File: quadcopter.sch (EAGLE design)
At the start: 58 parts, among them J1 AVR_SPI_PRG_6NS, U1 ATMEGA128RFA1

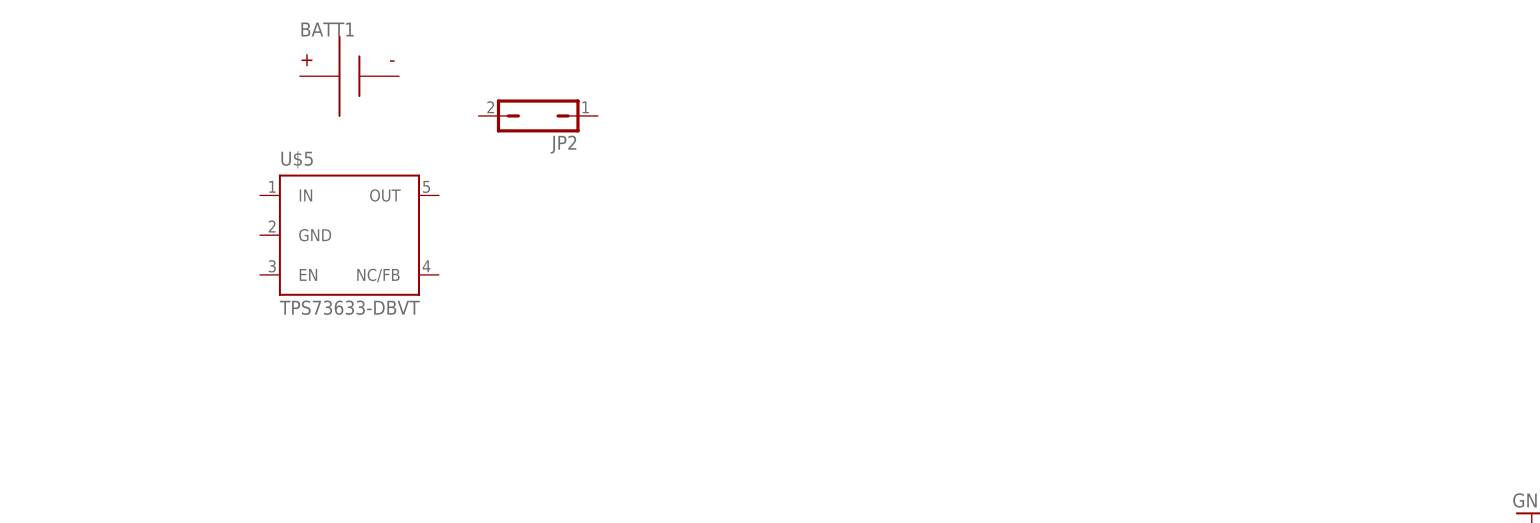
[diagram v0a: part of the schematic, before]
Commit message: Added breakout header and power-supply parts
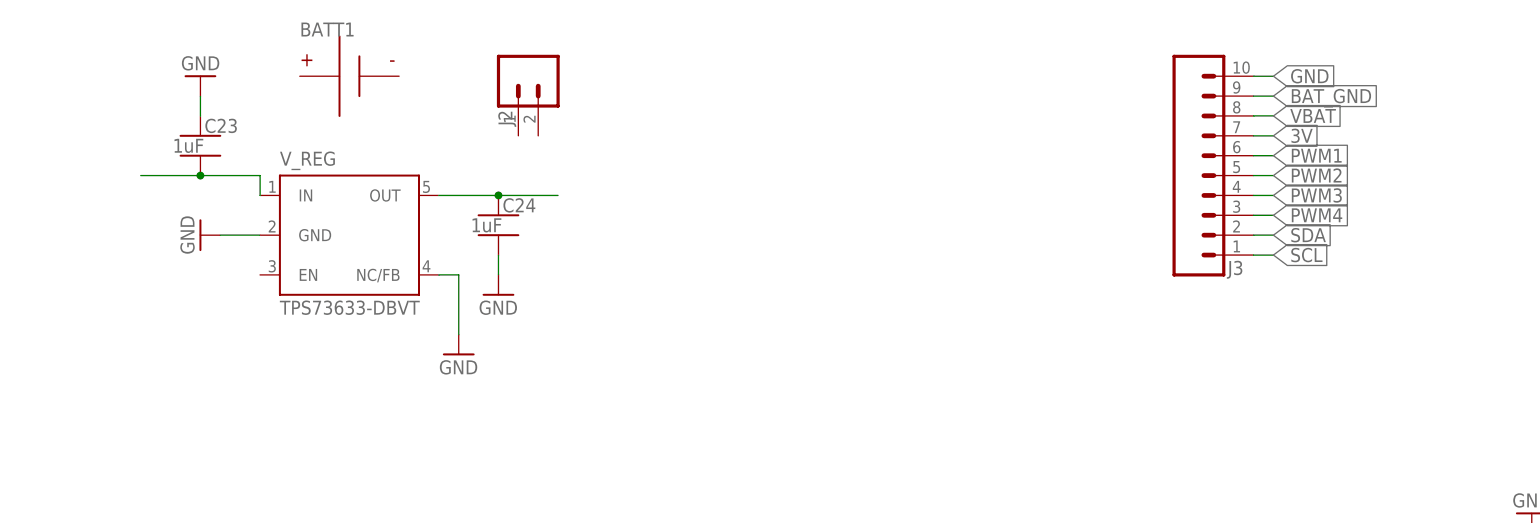
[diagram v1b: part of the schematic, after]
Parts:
- removed JP2: (no value), jumper:JP1Q
- added C23, C24: 1uF, quadparts_prebuilt:CAPACITOR-NP_SMD-2012-0805_CERAMIC-1UF
- added J2: (no value), quadparts-nick:MALE_HEADER_2POS-2X1-0.1IN
- added J3: (no value), quadparts_prebuilt:SIP-10_TH-254X10
- renumbered U$5 to V_REG
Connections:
- new net 3V: J3.7
- new net BAT_GND: J3.9
- new net N$16: C24.1, V_REG.OUT
- new net N$17: C23.2, V_REG.IN
- new net SCL: J3.1
- new net SDA: J3.2
- new net VBAT: J3.8
- net GND: now also C23.1, C24.2, J3.10, V_REG.GND, V_REG.NC/FB
- net PWM1: now also J3.6
- net PWM2: now also J3.5
- net PWM3: now also J3.4
- net PWM4: now also J3.3
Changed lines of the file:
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@@
 <part name="C20" library="quadparts_prebuilt" deviceset="CAPACITOR-NP_" device="SMD-2012-0805_CERAMIC-0.1UF" value="0.1uF"/>
 <part name="BATT1" library="quadparts_prebuilt" deviceset="BATTERY" device="-HUBSAN-W/HOLDER"/>
-<part name="U$5" library="quadparts_prebuilt" deviceset="TPS73633-DBVT" device=""/>
-<part name="JP2" library="jumper" deviceset="JP1Q" device=""/>
+<part name="V_REG" library="quadparts_prebuilt" deviceset="TPS73633-DBVT" device=""/>
+<part name="GND33" library="quadparts_prebuilt" deviceset="GND" device=""/>
+<part name="GND34" library="quadparts_prebuilt" deviceset="GND" device=""/>
+<part name="C23" library="quadparts_prebuilt" deviceset="CAPACITOR-NP_" device="SMD-2012-0805_CERAMIC-1UF" value="1uF"/>
+<part name="C24" library="quadparts_prebuilt" deviceset="CAPACITOR-NP_" device="SMD-2012-0805_CERAMIC-1UF" value="1uF"/>
+<part name="GND35" library="quadparts_prebuilt" deviceset="GND" device=""/>
+<part name="GND36" library="quadparts_prebuilt" deviceset="GND" device=""/>
+<part name="J2" library="quadparts-nick" deviceset="MALE_HEADER_2POS" device="-2X1-0.1IN"/>
+<part name="J3" library="quadparts_prebuilt" deviceset="SIP-10_" device="TH-254X10"/>
 </parts>
 <sheets>
@@
 <instance part="C20" gate="G$1" x="160.02" y="2.54"/>
 <instance part="BATT1" gate="G$1" x="-101.6" y="60.96"/>
-<instance part="U$5" gate="G$1" x="-111.76" y="33.02"/>
-<instance part="JP2" gate="A" x="-78.74" y="55.88" rot="R90"/>
+<instance part="V_REG" gate="G$1" x="-111.76" y="33.02"/>
+<instance part="GND33" gate="1" x="-121.92" y="40.64" rot="R270"/>
+<instance part="GND34" gate="1" x="-88.9" y="25.4"/>
+<instance part="C23" gate="G$1" x="-121.92" y="53.34"/>
+<instance part="C24" gate="G$1" x="-83.82" y="43.18"/>
+<instance part="GND35" gate="1" x="-121.92" y="60.96" rot="R180"/>
+<instance part="GND36" gate="1" x="-83.82" y="33.02"/>
+<instance part="J2" gate="G$1" x="-83.82" y="63.5" rot="R270"/>
+<instance part="J3" gate="G$1" x="2.54" y="35.56"/>
 </instances>
 <busses>
@@
 <wire x1="147.32" y1="-25.4" x2="147.32" y2="-27.94" width="0.1524" layer="91"/>
 </segment>
+<segment>
+<pinref part="GND33" gate="1" pin="GND"/>
+<pinref part="V_REG" gate="G$1" pin="GND"/>
+<wire x1="-119.38" y1="40.64" x2="-114.3" y2="40.64" width="0.1524" layer="91"/>
+</segment>
+<segment>
+<pinref part="V_REG" gate="G$1" pin="NC/FB"/>
+<pinref part="GND34" gate="1" pin="GND"/>
+<wire x1="-91.44" y1="35.56" x2="-88.9" y2="35.56" width="0.1524" layer="91"/>
+<wire x1="-88.9" y1="35.56" x2="-88.9" y2="27.94" width="0.1524" layer="91"/>
+</segment>
+<segment>
+<pinref part="C23" gate="G$1" pin="1"/>
+<pinref part="GND35" gate="1" pin="GND"/>
+<wire x1="-121.92" y1="55.88" x2="-121.92" y2="58.42" width="0.1524" layer="91"/>
+</segment>
+<segment>
+<pinref part="C24" gate="G$1" pin="2"/>
+<pinref part="GND36" gate="1" pin="GND"/>
+<wire x1="-83.82" y1="38.1" x2="-83.82" y2="35.56" width="0.1524" layer="91"/>
+</segment>
+<segment>
+<pinref part="J3" gate="G$1" pin="10"/>
+<wire x1="12.7" y1="60.96" x2="15.24" y2="60.96" width="0.1524" layer="91"/>
+<label x="15.24" y="60.96" size="1.778" layer="95" xref="yes"/>
+</segment>
 </net>
 <net name="N$2" class="0">
@@
 <label x="-81.28" y="-78.74" size="1.778" layer="95" rot="R180" xref="yes"/>
 </segment>
+<segment>
+<pinref part="J3" gate="G$1" pin="3"/>
+<wire x1="12.7" y1="43.18" x2="15.24" y2="43.18" width="0.1524" layer="91"/>
+<label x="15.24" y="43.18" size="1.778" layer="95" xref="yes"/>
+</segment>
 </net>
 <net name="FLYBACK" class="0">
@@
 <label x="-81.28" y="-33.02" size="1.778" layer="95" rot="R180" xref="yes"/>
 </segment>
+<segment>
+<pinref part="J3" gate="G$1" pin="6"/>
+<wire x1="12.7" y1="50.8" x2="15.24" y2="50.8" width="0.1524" layer="91"/>
+<label x="15.24" y="50.8" size="1.778" layer="95" xref="yes"/>
+</segment>
 </net>
 <net name="PWM2" class="0">
@@
 <label x="-81.28" y="-35.56" size="1.778" layer="95" rot="R180" xref="yes"/>
 </segment>
+<segment>
+<pinref part="J3" gate="G$1" pin="5"/>
+<wire x1="12.7" y1="48.26" x2="15.24" y2="48.26" width="0.1524" layer="91"/>
+<label x="15.24" y="48.26" size="1.778" layer="95" xref="yes"/>
+</segment>
 </net>
 <net name="PWM3" class="0">
@@
 <label x="-81.28" y="-38.1" size="1.778" layer="95" rot="R180" xref="yes"/>
 </segment>
+<segment>
+<pinref part="J3" gate="G$1" pin="4"/>
+<wire x1="12.7" y1="45.72" x2="15.24" y2="45.72" width="0.1524" layer="91"/>
+<label x="15.24" y="45.72" size="1.778" layer="95" xref="yes"/>
+</segment>
 </net>
 <net name="N$13" class="0">
@@
 </segment>
 </net>
+<net name="N$16" class="0">
+<segment>
+<pinref part="V_REG" gate="G$1" pin="OUT"/>
+<wire x1="-91.44" y1="45.72" x2="-83.82" y2="45.72" width="0.1524" layer="91"/>
+<pinref part="C24" gate="G$1" pin="1"/>
+<junction x="-83.82" y="45.72"/>
+<wire x1="-83.82" y1="45.72" x2="-76.2" y2="45.72" width="0.1524" layer="91"/>
+</segment>
+</net>
+<net name="N$17" class="0">
+<segment>
+<pinref part="V_REG" gate="G$1" pin="IN"/>
+<wire x1="-114.3" y1="45.72" x2="-114.3" y2="48.26" width="0.1524" layer="91"/>
+<wire x1="-114.3" y1="48.26" x2="-121.92" y2="48.26" width="0.1524" layer="91"/>
+<pinref part="C23" gate="G$1" pin="2"/>
+<junction x="-121.92" y="48.26"/>
+<wire x1="-121.92" y1="48.26" x2="-129.54" y2="48.26" width="0.1524" layer="91"/>
+</segment>
+</net>
+<net name="BAT_GND" class="0">
+<segment>
+<pinref part="J3" gate="G$1" pin="9"/>
+<wire x1="12.7" y1="58.42" x2="15.24" y2="58.42" width="0.1524" layer="91"/>
+<label x="15.24" y="58.42" size="1.778" layer="95" xref="yes"/>
+</segment>
+</net>
+<net name="VBAT" class="0">
+<segment>
+<pinref part="J3" gate="G$1" pin="8"/>
+<wire x1="12.7" y1="55.88" x2="15.24" y2="55.88" width="0.1524" layer="91"/>
+<label x="15.24" y="55.88" size="1.778" layer="95" xref="yes"/>
+</segment>
+</net>
+<net name="3V" class="0">
+<segment>
+<pinref part="J3" gate="G$1" pin="7"/>
+<wire x1="12.7" y1="53.34" x2="15.24" y2="53.34" width="0.1524" layer="91"/>
+<label x="15.24" y="53.34" size="1.778" layer="95" xref="yes"/>
+</segment>
+</net>
+<net name="SDA" class="0">
+<segment>
+<pinref part="J3" gate="G$1" pin="2"/>
+<wire x1="12.7" y1="40.64" x2="15.24" y2="40.64" width="0.1524" layer="91"/>
+<label x="15.24" y="40.64" size="1.778" layer="95" xref="yes"/>
+</segment>
+</net>
+<net name="SCL" class="0">
+<segment>
+<pinref part="J3" gate="G$1" pin="1"/>
+<wire x1="12.7" y1="38.1" x2="15.24" y2="38.1" width="0.1524" layer="91"/>
+<label x="15.24" y="38.1" size="1.778" layer="95" xref="yes"/>
+</segment>
+</net>

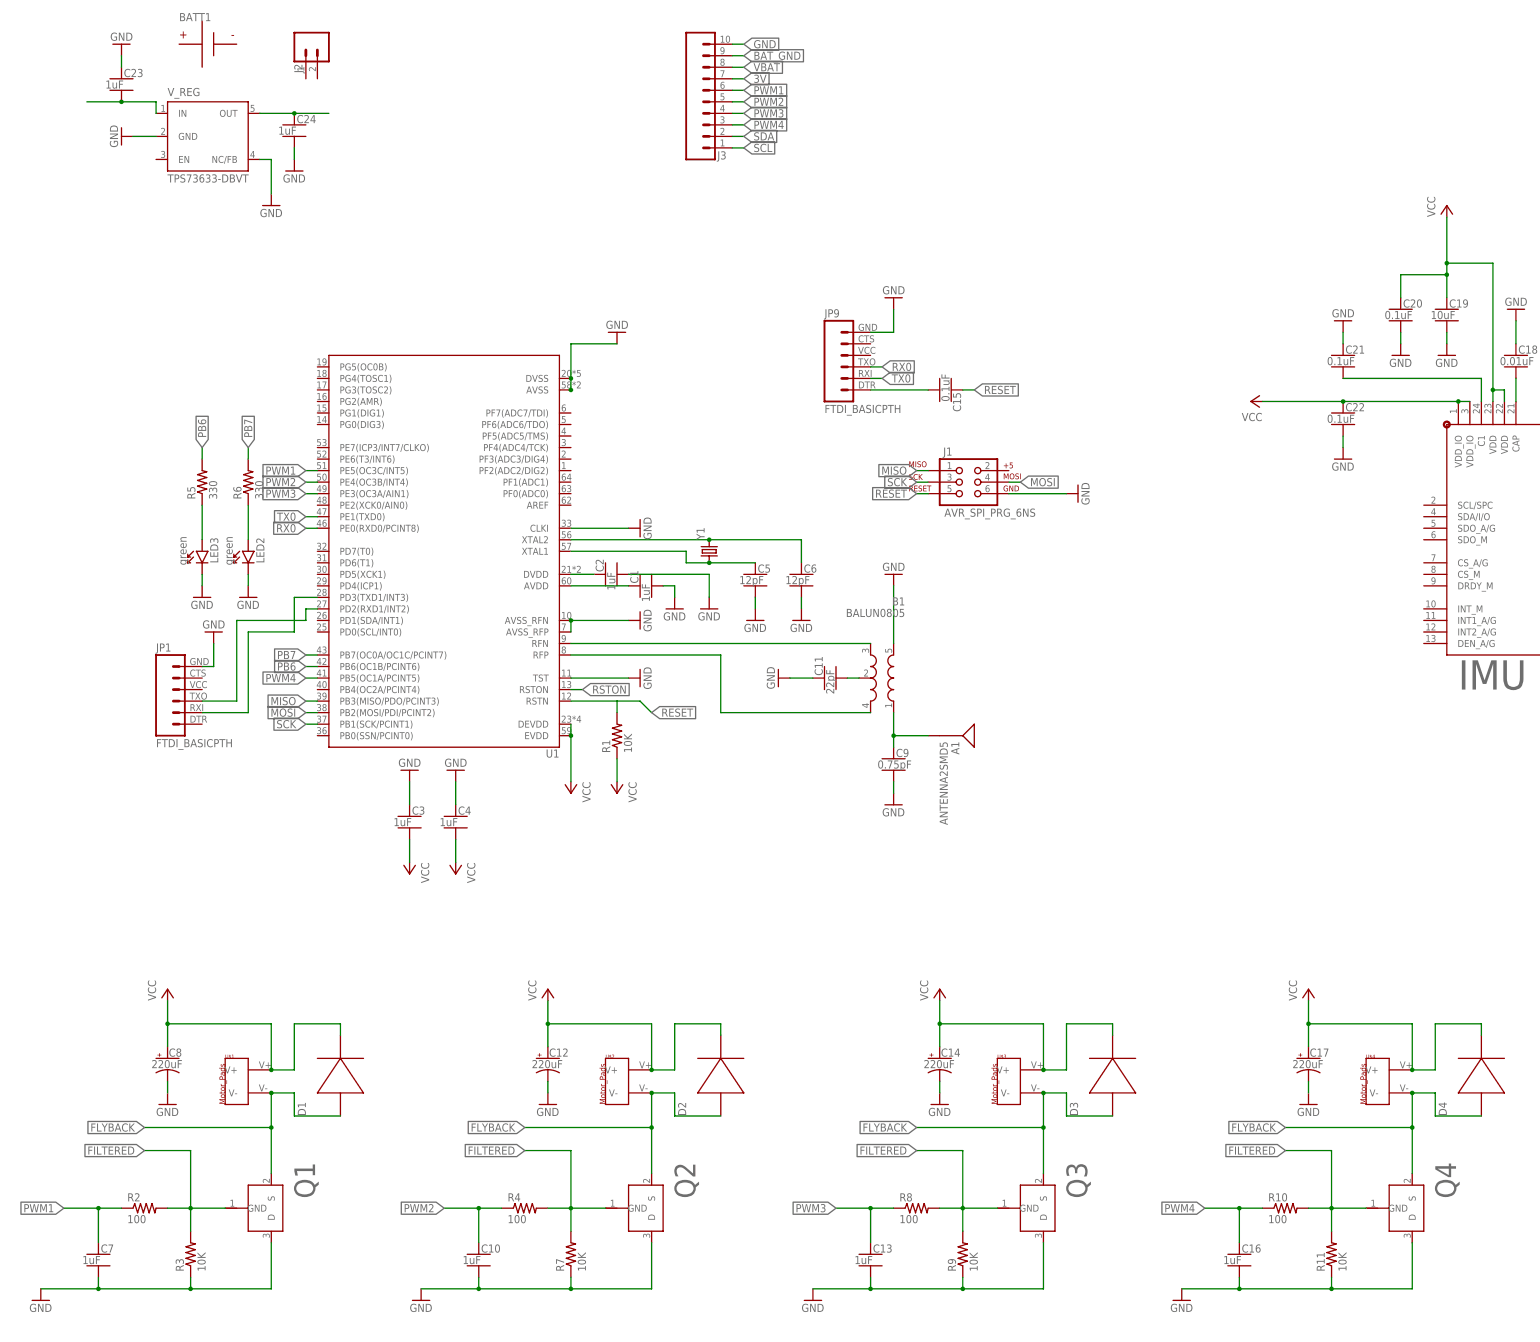
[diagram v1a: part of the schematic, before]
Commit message: Hooked up power supply, fixed some connections on IMU
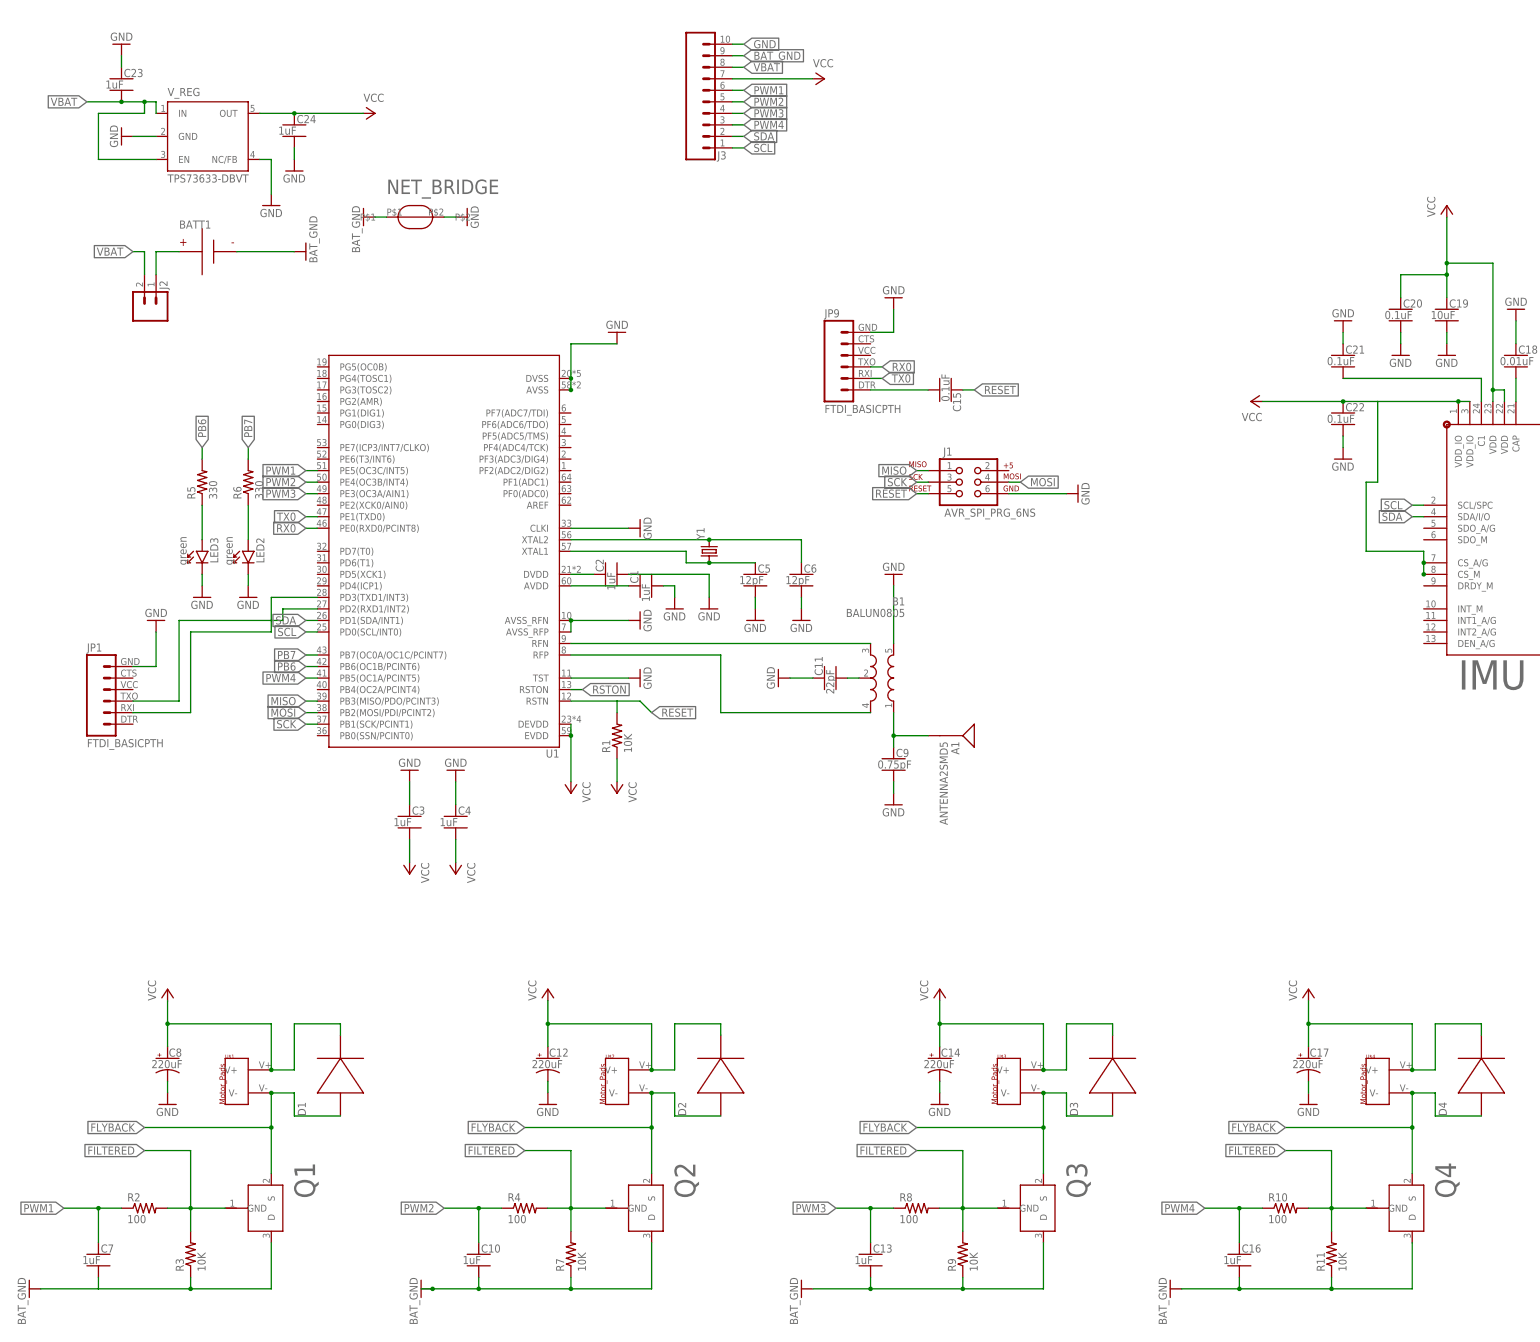
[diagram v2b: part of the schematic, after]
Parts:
- added NET_BRIDGE: NET_BRIDGE, quadparts-nick:NET_BRIDGE
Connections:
- removed net 3V: J3.7
- removed net N$16: C24.1, V_REG.OUT
- removed net N$17: C23.2, V_REG.IN
- new net N$18: BATT1.P, J2.1
- net BAT_GND: now also BATT1.N, C10.2, C13.2, C16.2, C7.2, NET_BRIDGE.P$1, Q1.D, Q2.D, Q3.D, Q4.D, R11.1, R3.1, R7.1, R9.1
- net GND: now also NET_BRIDGE.P$2; no longer C10.2, C13.2, C16.2, C7.2, Q1.D, Q2.D, Q3.D, Q4.D, R11.1, R3.1, R7.1, R9.1
- net SCL: now also IMU.SCL/SPC, U1.PD0(SCL/INT0)
- net SDA: now also IMU.SDA/I/O, U1.PD1(SDA/INT1)
- net VBAT: now also C23.2, J2.2, V_REG.EN, V_REG.IN
- net VCC: now also C24.1, IMU.CS_A/G, IMU.CS_M, J3.7, V_REG.OUT
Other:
- moved on the sheet: BATT1, J2, JP1

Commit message: fixed a few nets
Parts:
- D1, D2, D3, D4: value (none) -> RED
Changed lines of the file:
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@@
 <part name="R3" library="quadparts_prebuilt" deviceset="RESISTOR_" device="SMD-2012-0805-10K" value="10K"/>
 <part name="C7" library="quadparts_prebuilt" deviceset="CAPACITOR-NP_" device="SMD-2012-0805_CERAMIC-1UF" value="1uF"/>
-<part name="D1" library="quadparts-nick" deviceset="RED_LED" device=""/>
+<part name="D1" library="quadparts-nick" deviceset="RED_LED" device="" value="RED"/>
 <part name="U$1" library="quadparts_prebuilt" deviceset="MOTOR_PADS" device=""/>
 <part name="P+1" library="quadparts_prebuilt" deviceset="VCC" device=""/>
@@
 <part name="R7" library="quadparts_prebuilt" deviceset="RESISTOR_" device="SMD-2012-0805-10K" value="10K"/>
 <part name="C10" library="quadparts_prebuilt" deviceset="CAPACITOR-NP_" device="SMD-2012-0805_CERAMIC-1UF" value="1uF"/>
-<part name="D2" library="quadparts-nick" deviceset="RED_LED" device=""/>
+<part name="D2" library="quadparts-nick" deviceset="RED_LED" device="" value="RED"/>
 <part name="U$2" library="quadparts_prebuilt" deviceset="MOTOR_PADS" device=""/>
 <part name="P+2" library="quadparts_prebuilt" deviceset="VCC" device=""/>
@@
 <part name="R9" library="quadparts_prebuilt" deviceset="RESISTOR_" device="SMD-2012-0805-10K" value="10K"/>
 <part name="C13" library="quadparts_prebuilt" deviceset="CAPACITOR-NP_" device="SMD-2012-0805_CERAMIC-1UF" value="1uF"/>
-<part name="D3" library="quadparts-nick" deviceset="RED_LED" device=""/>
+<part name="D3" library="quadparts-nick" deviceset="RED_LED" device="" value="RED"/>
 <part name="U$3" library="quadparts_prebuilt" deviceset="MOTOR_PADS" device=""/>
 <part name="P+3" library="quadparts_prebuilt" deviceset="VCC" device=""/>
@@
 <part name="R11" library="quadparts_prebuilt" deviceset="RESISTOR_" device="SMD-2012-0805-10K" value="10K"/>
 <part name="C16" library="quadparts_prebuilt" deviceset="CAPACITOR-NP_" device="SMD-2012-0805_CERAMIC-1UF" value="1uF"/>
-<part name="D4" library="quadparts-nick" deviceset="RED_LED" device=""/>
+<part name="D4" library="quadparts-nick" deviceset="RED_LED" device="" value="RED"/>
 <part name="U$4" library="quadparts_prebuilt" deviceset="MOTOR_PADS" device=""/>
 <part name="P+4" library="quadparts_prebuilt" deviceset="VCC" device=""/>
@@
 <wire x1="165.1" y1="-53.34" x2="165.1" y2="-55.88" width="0.1524" layer="91"/>
 <junction x="165.1" y="-55.88"/>
+<junction x="154.94" y="-17.78"/>
 </segment>
 <segment>
@@
 <wire x1="-7.62" y1="-83.82" x2="-5.08" y2="-86.36" width="0.1524" layer="91"/>
 <label x="-5.08" y="-86.36" size="1.778" layer="95" xref="yes"/>
+<junction x="-12.7" y="-83.82"/>
 </segment>
 <segment>
@@
 <pinref part="GND19" gate="1" pin="BAT_GND"/>
 <wire x1="-127" y1="-213.36" x2="-139.7" y2="-213.36" width="0.1524" layer="91"/>
+<junction x="-127" y="-213.36"/>
 </segment>
 <segment>
@@
 </sheet>
 </sheets>
+<errors>
+</errors>
 </schematic>
 </drawing>
